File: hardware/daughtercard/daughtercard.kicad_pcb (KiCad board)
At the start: 2 copper layers, 74 x 60 mm, 52 parts, among them J1 Anzeige, J2 Bus in, J3 Bus out, J4 42V~ in, J5 42V~ out, J6 UPDI, Q1 BSS84, Q2 MMBT3904, Q3 MMBT3904, U1 ATtiny1616-SNR, U2 TP8485E-SR

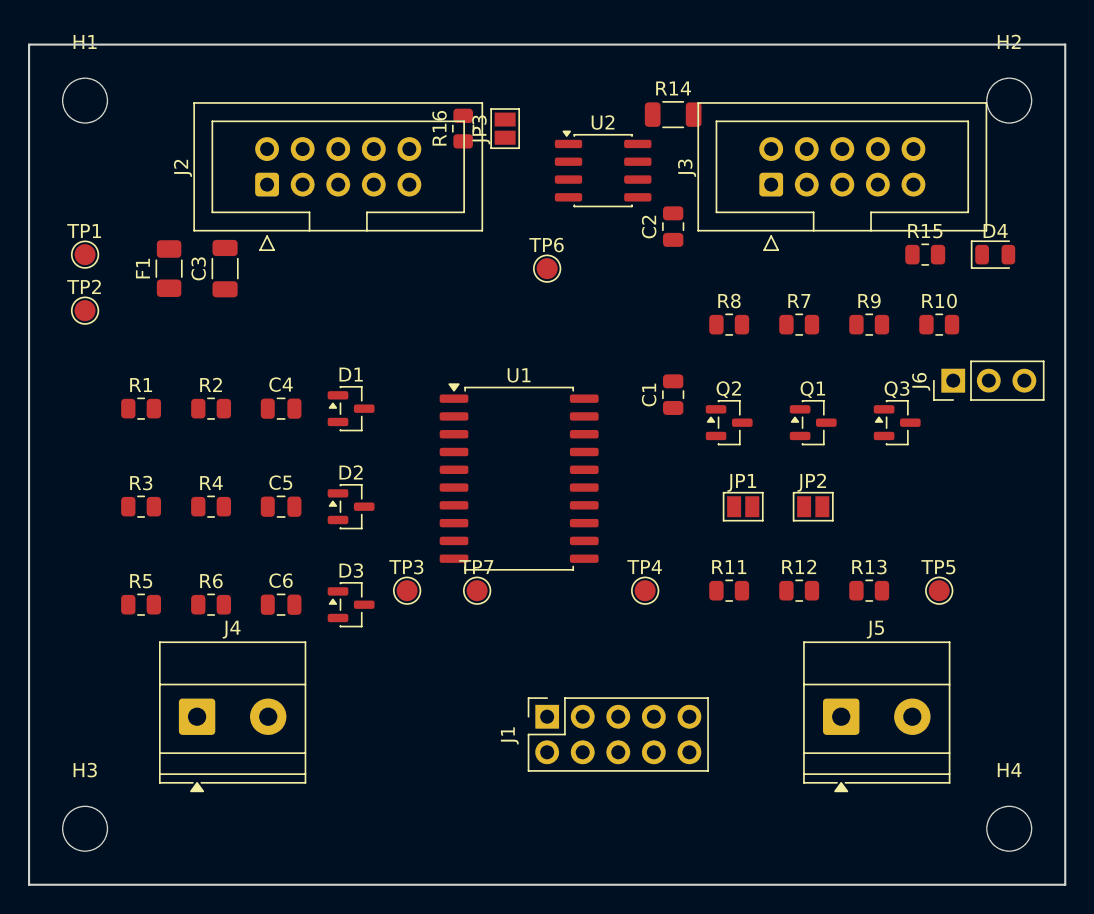
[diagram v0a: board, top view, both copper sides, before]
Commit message: Update part placement
Manuelle Anpassung der Bauteilplatzierung.
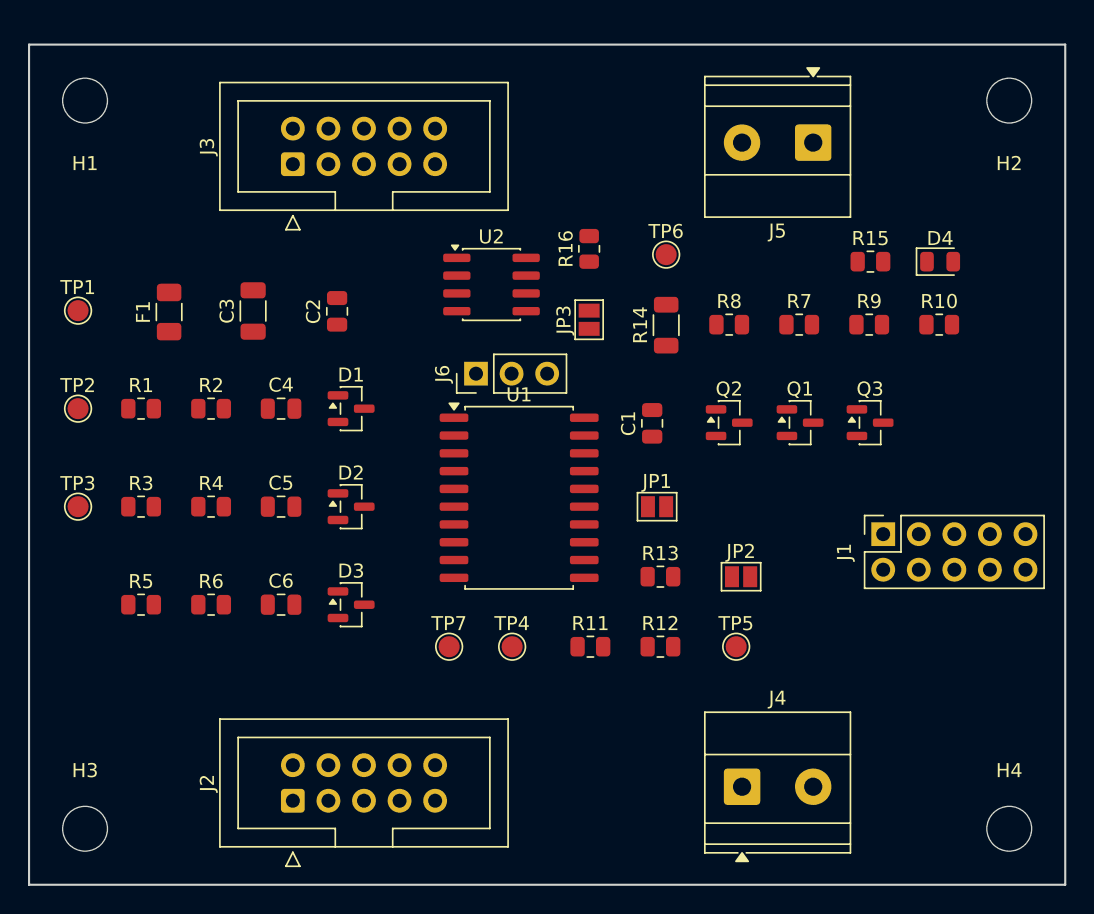
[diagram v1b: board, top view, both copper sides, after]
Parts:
- moved J2 44.0 mm to (18.8, 54.0)
- moved J5 41.0 mm to (56.0, 7.00), turned to 180 degrees
- moved J4 39.2 mm to (50.9, 53.0)
- moved J3 34.2 mm to (18.8, 8.54)
- moved J6 34.1 mm to (31.9, 23.5)
- moved J1 27.3 mm to (61.0, 35.0)
- moved C2 24.8 mm to (22.0, 19.1)
- moved TP3 24.3 mm to (3.50, 33.0)
- moved R14 15.0 mm to (45.5, 20.0), turned to 90 degrees
- moved TP5 15.0 mm to (50.5, 43.0)
- moved R13 14.9 mm to (45.1, 38.0)
- moved JP3 14.9 mm to (40.0, 19.6)
- moved R16 12.4 mm to (40.0, 14.6)
- moved U2 11.4 mm to (33.0, 17.1)
- moved R11 10.7 mm to (40.1, 43.0)
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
